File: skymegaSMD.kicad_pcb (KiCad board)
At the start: 2 copper layers, 49 x 49 mm, 56 parts, among them IC1 ATMEGA328P-A, K1 CONN_3, P1 CONN_2, P2 CONN_2, SW1 SWITCH On_Off, SW2 SW_PUSH, SW3 SW_PUSH, U1 MIC5205, X1 16Mhz

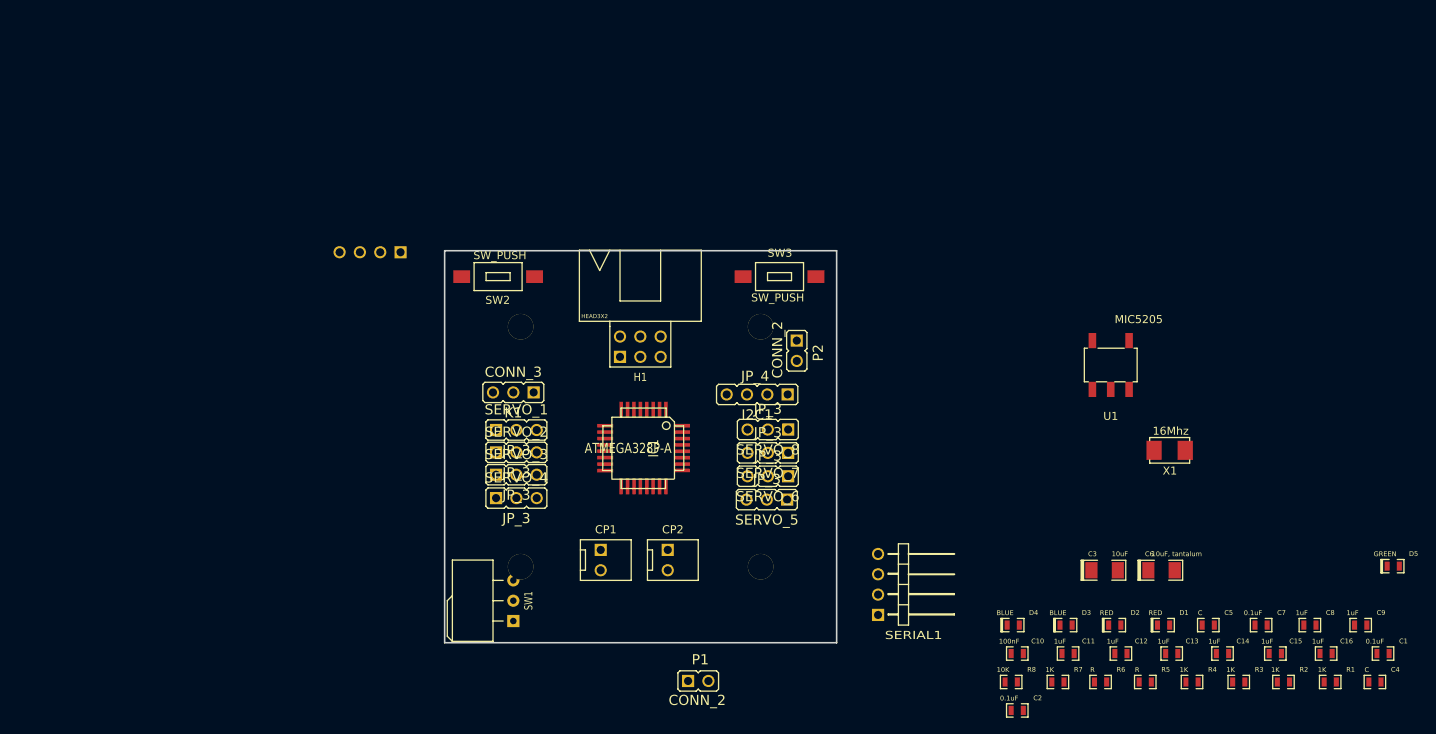
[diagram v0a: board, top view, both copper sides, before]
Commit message: All components placed, capacitors bug solved.
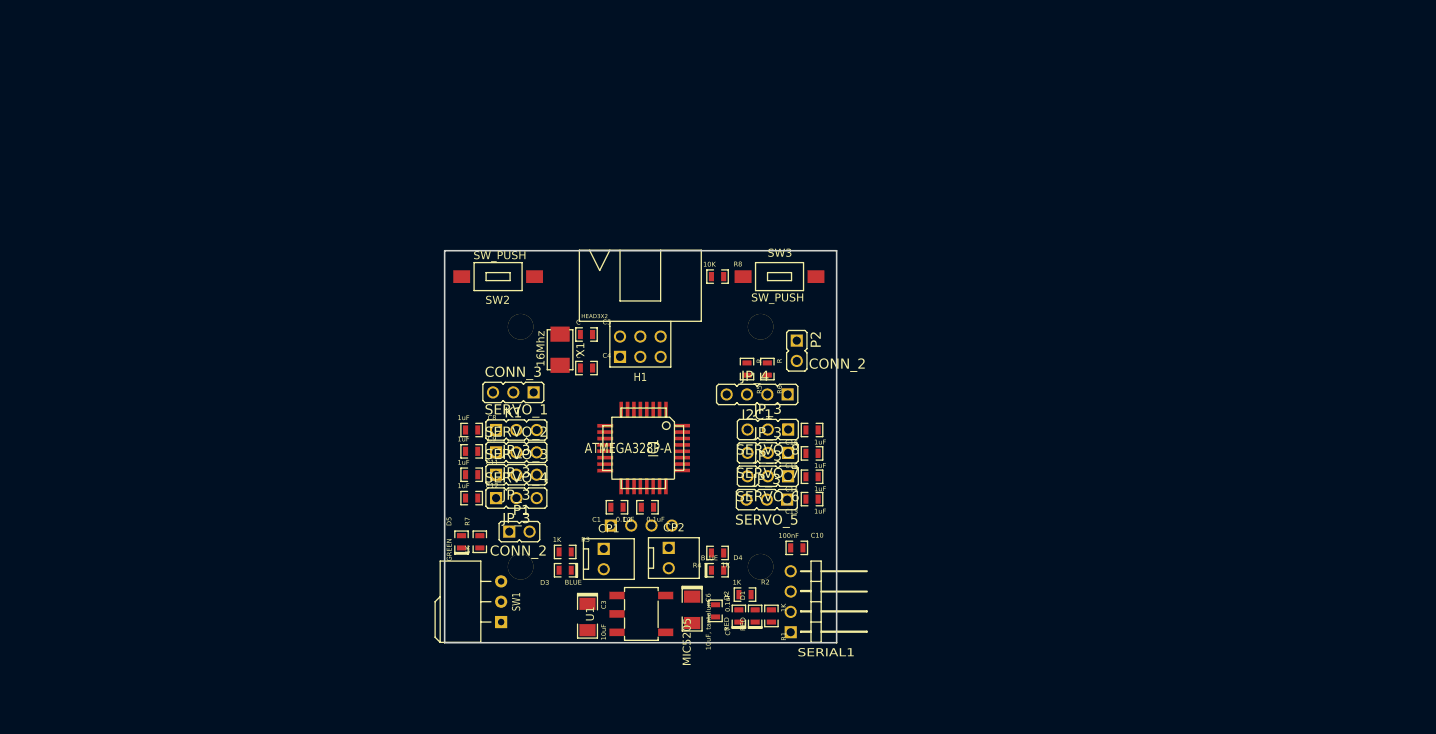
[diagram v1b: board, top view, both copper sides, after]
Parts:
- moved D5 116.5 mm to (175.9, 148.1), turned to 90 degrees
- moved C9 113.2 mm to (177.2, 136.8)
- moved C8 107.6 mm to (177.2, 134.1)
- moved C4 106.1 mm to (191.5, 126.4)
- moved C1 97.5 mm to (195.3, 143.8), turned to 180 degrees
- moved C5 85.8 mm to (191.5, 122.2)
- moved R3 85.8 mm to (188.8, 149.4)
- moved C12 83.4 mm to (177.2, 142.6)
- moved C11 77.8 mm to (177.2, 139.7)
- moved X1 77.2 mm to (188.2, 124.1), turned to 90 degrees
- moved R7 74.4 mm to (178.2, 148.1), turned to 90 degrees
- moved R1 70.3 mm to (214.6, 157.4), turned to 270 degrees
- moved C16 70.1 mm to (219.7, 134.1), turned to 180 degrees
- moved C7 68.2 mm to (207.6, 156.7), turned to 270 degrees
- moved R2 68.2 mm to (211.3, 154.7)
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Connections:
- C13 pad 1: GND -> /Vin
- C14 pad 1: GND -> /Vin
- C8 pad 1: GND -> /Vin
- C9 pad 1: GND -> /Vin

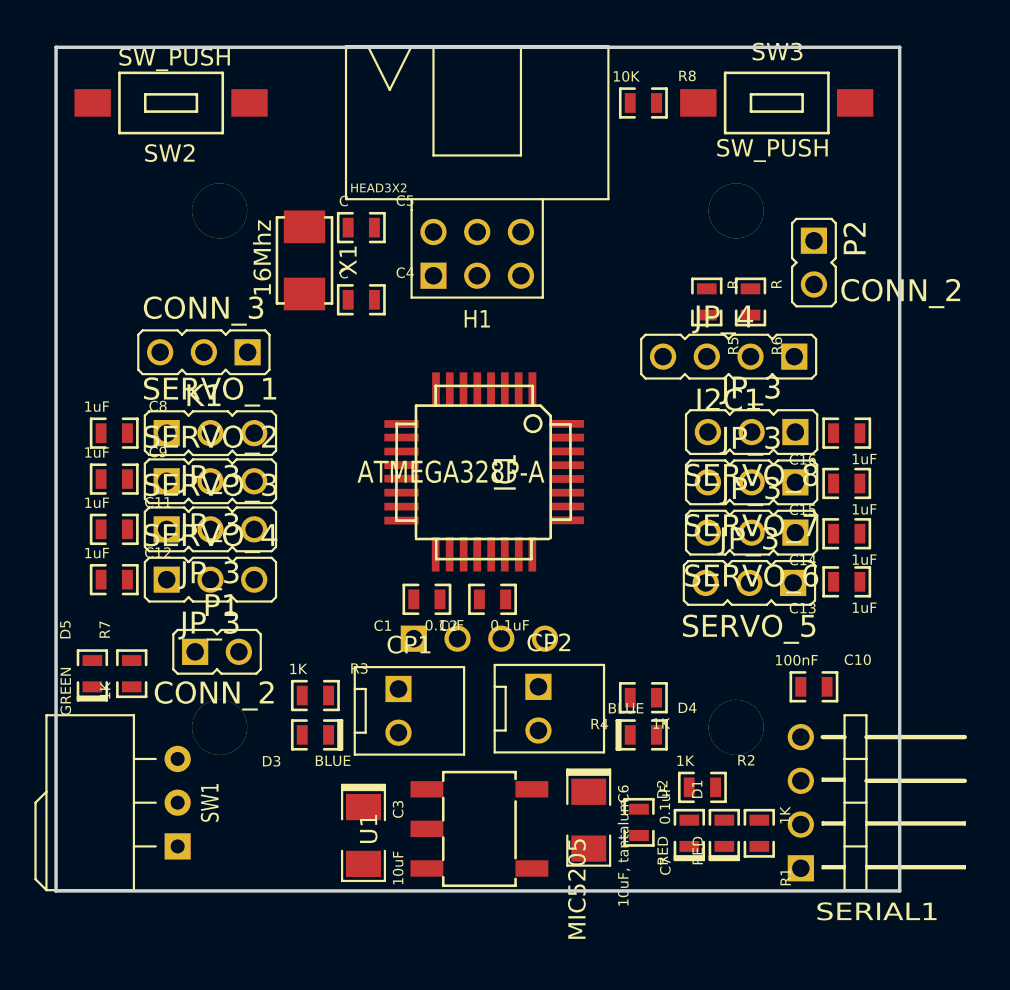
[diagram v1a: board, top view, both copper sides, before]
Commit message: More things routed.
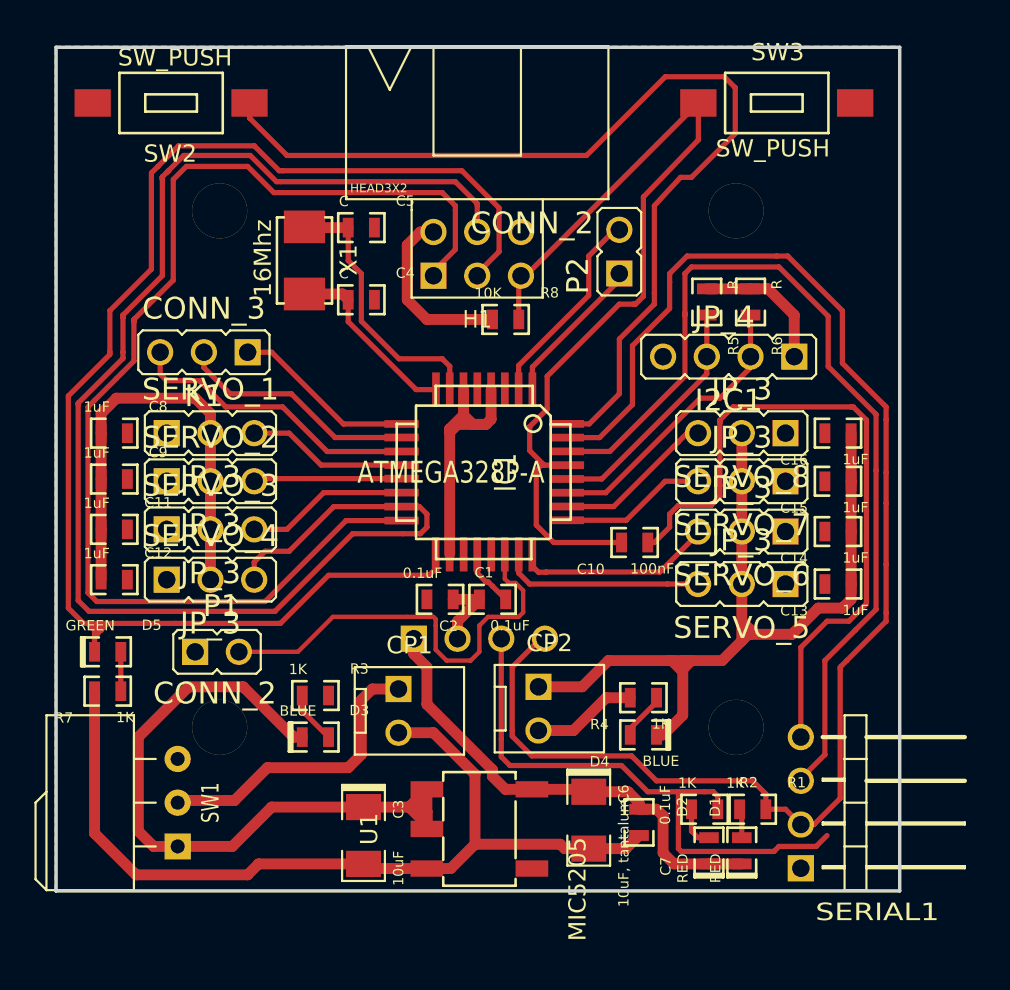
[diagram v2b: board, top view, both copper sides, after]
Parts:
- moved R8 14.9 mm to (199.9, 127.5)
- moved C10 13.4 mm to (207.4, 140.5), turned to 180 degrees
- moved P2 11.5 mm to (206.5, 124.8), turned to 90 degrees
- moved R7 1.73 mm to (176.8, 149.1), turned to 180 degrees
- moved D5 1.55 mm to (176.8, 146.8), turned to 0 degrees
- moved D2 1.53 mm to (211.7, 158.4)
- moved R1 1.45 mm to (214.2, 156.0), turned to 0 degrees
- moved D1 1.44 mm to (213.6, 158.4)
- moved R2 1.28 mm to (211.5, 156.0)
- moved C1 0.76 mm to (196.1, 143.8), turned to 0 degrees
- moved SERVO_6 0.58 mm to (216.2, 139.8)
- moved SERVO_7 0.58 mm to (216.2, 136.9)
- moved SERVO_8 0.58 mm to (216.2, 134.1)
- moved C13 0.52 mm to (219.2, 142.9)
- moved C14 0.52 mm to (219.2, 139.8)
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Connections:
- C13 pad 1: /Vin -> /SERVO_PWR_2
- C14 pad 1: /Vin -> /SERVO_PWR_2
- C15 pad 1: /Vin -> /SERVO_PWR_2
- C16 pad 1: /Vin -> /SERVO_PWR_2
- SERVO_5 pad 2: /Vin -> /SERVO_PWR_2
- SERVO_6 pad 2: /Vin -> /SERVO_PWR_2
- SERVO_7 pad 2: /Vin -> /SERVO_PWR_2
- SERVO_8 pad 2: /Vin -> /SERVO_PWR_2
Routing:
- net /RX: track 0.00 -> 87.9 mm
- net /D11: track 0.00 -> 85.0 mm
- net /TX: track 0.00 -> 84.3 mm
- net /D13: track 0.00 -> 82.6 mm
- net /D12: track 0.00 -> 68.9 mm
- net /Vin: track 0.00 -> 68.2 mm
- net VCC: track 0.00 -> 62.3 mm
- net GND: track 0.00 -> 62.2 mm
- net /D2: track 0.00 -> 56.8 mm
- net /RESET: track 0.00 -> 53.5 mm
- net /SERVO_PWR_2: track 0.00 -> 50.1 mm
- net /DTR: track 0.00 -> 40.2 mm
- net /A7: track 0.00 -> 25.5 mm
- net N-000006: track 0.00 -> 17.4 mm
- net /D7: track 0.00 -> 17.2 mm
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- added copper zone on B.Cu, net GND
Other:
- net class Power added: clearance 0.254, trace_width 0.635, via_dia 0.889, via_drill 0.635
- net class Thick added: clearance 0.254, trace_width 0.3048, via_dia 0.889, via_drill 0.635

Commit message: Only a line left.
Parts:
- moved C1 4.18 mm to (192.2, 145.2), turned to 90 degrees
- moved R8 1.91 mm to (198.0, 127.5)
- moved P1 0.51 mm to (181.9, 147.3)
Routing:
- net GND: track 62.2 -> 235.0 mm
- net VCC: track 62.3 -> 129.4 mm, vias 0 -> 1
- net /A6: track 0.00 -> 19.1 mm
- net /Vin: track 68.2 -> 83.0 mm, vias 0 -> 2
- net /D2: track 56.8 -> 53.8 mm
- net /D13: track 82.6 -> 81.5 mm
- net /RESET: track 53.5 -> 54.5 mm
- net /D12: track 68.9 -> 70.0 mm
- net /D11: track 85.0 -> 86.0 mm

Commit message: Production PCB
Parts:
- added G***: OSHW-logo, OSHW-logo, F.Cu at (125.6, 93.2)
- added G***: LOGO, LOGO_15x15, B.Cu at (145.9, 105.5)
- C6: value 10uF, tantalum -> 10uF
- moved C10 62.0 mm to (152.4, 111.8)
- moved D3 60.2 mm to (136.3, 122.4)
- moved R3 60.2 mm to (136.3, 120.0)
- moved C1 59.9 mm to (139.8, 116.0)
- moved C13 59.9 mm to (166.9, 113.7)
- moved C14 59.9 mm to (166.9, 110.6)
- moved C16 59.9 mm to (166.9, 104.9)
- moved C7 59.9 mm to (155.3, 127.5)
- moved CP1 59.9 mm to (141.4, 119.8)
- moved D1 59.9 mm to (161.3, 129.2)
- moved D2 59.9 mm to (159.4, 129.2)
- moved D4 59.9 mm to (155.6, 122.4)
- moved I2C 59.9 mm to (164.3, 100.5)
- moved K1 59.9 mm to (132.6, 100.2)
- moved P1 59.9 mm to (129.5, 118.1)
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- renumbered I2C1 to I2C
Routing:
- net GND: track 235.0 -> 214.4 mm
- net /RESET: track 54.5 -> 52.1 mm
- net /DTR: track 40.2 -> 42.0 mm
- net /RX: track 87.9 -> 89.6 mm, vias 0 -> 1
- net /Vin: track 83.0 -> 84.7 mm
- net N-0000034: track 10.7 -> 11.2 mm
- added copper zone on F.Cu, net GND
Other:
- outline, holes or cut-outs redrawn
- rule trace_min: 0.254 -> 0.1524
- board text added: "(SCL)A5"
- board text added: "+ Vin -"
- board text added: "+ Vout -"
- board text added: "A0"
- board text added: "A1"
- board text added: "A2"
- board text added: "A3"
- board text added: "A4"
- board text added: "A4(SDA)"
- board text added: "A5"
- board text added: "A6"
- board text added: "A7"
- board text added: "Based on Skymega Board"
- board text added: "CTRL"
- board text added: "D10"
- board text added: "D11"
- board text added: "D12"
- board text added: "D13"
- board text added: "D4"
- board text added: "D5"
- board text added: "D6"
- board text added: "D7"
- board text added: "D8"
- board text added: "D9"
- board text added: "DTR"
- board text added: "Designed by: David Estevez Fernandez"
- board text added: "GND"
- board text added: "GPLv3"
- board text added: "RESET"
- board text added: "RST"
- board text added: "Rx"
- board text added: "SERVO 1"
- board text added: "SERVO 2"
- board text added: "SERVO 3"
- board text added: "SERVO 4"
- board text added: "SERVO5"
- board text added: "SERVO6"
- board text added: "SERVO7"
- board text added: "SERVO8"
- board text added: "SkymegaSMD v1.0 (beta)"
- board text added: "Tx"
- board text added: "USER (D2)"
- board text added: "USER LED"
- board text added: "VCC"
- board text added: "VCC1"
- board text added: "VCC2"
- board text added: "Vin"
- board text added: "www.dsquaredrobotics.com/wiki/doku.php?id=en:repy-2.0"

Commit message: Version presented on thesis.
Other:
- rule pad_to_mask_clearance: 0 -> 0.1
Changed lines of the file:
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@@
     (pad_size 1 1)
     (pad_drill 0.6)
-    (pad_to_mask_clearance 0)
+    (pad_to_mask_clearance 0.1)
+    (solder_mask_min_width 0.1)
     (aux_axis_origin 0 0)
     (visible_elements 7FFFFBBF)
     (pcbplotparams
-      (layerselection 3178497)
+      (layerselection 284196865)
       (usegerberextensions true)
-      (excludeedgelayer true)
-      (linewidth 150000)
+      (excludeedgelayer false)
+      (linewidth 20000)
       (plotframeref false)
       (viasonmask false)
@@
       (plotinvisibletext false)
       (padsonsilk false)
-      (subtractmaskfromsilk false)
+      (subtractmaskfromsilk true)
       (outputformat 1)
       (mirror false)
-      (drillshape 1)
+      (drillshape 0)
       (scaleselection 1)
-      (outputdirectory ""))
+      (outputdirectory Gerbers/))
   )
   (net 0 "")

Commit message: Some bugs solved.
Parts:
- C6: value 10uF -> 10uF, tantalum
- U1: footprint hebi_SOT-223-5 -> hebi_power-SOT-23-5
- moved X1 5.97 mm to (138.8, 100.1), turned to 0 degrees
- moved C5 4.02 mm to (140.5, 96.8), turned to 90 degrees
- moved C6 2.79 mm to (149.6, 127.4)
- moved C7 2.79 mm to (152.5, 127.5)
- moved C3 2.45 mm to (141.6, 127.4)
- moved C4 2.32 mm to (136.9, 96.8), turned to 90 degrees
- moved U1 1.17 mm to (145.3, 127.0)
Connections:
- SW1 pad 3: N-0000036 -> (no net)
- U1 pad 4: N-0000038 -> (no net)
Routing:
- net VCC: track 129.0 -> 120.9 mm
- net N-0000035: track 15.9 -> 7.90 mm
- net /D12: track 70.0 -> 64.4 mm
- net /D11: track 86.0 -> 80.5 mm
- net /D13: track 81.5 -> 76.7 mm
- net /Vin: track 84.7 -> 81.2 mm
- net GND: track 214.4 -> 212.6 mm, vias 0 -> 1
- net /D5: track 10.7 -> 11.2 mm
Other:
- board text added: "+"
- board text added: "-"
- board text removed: "+ Vin -"
- board text removed: "+ Vout -"

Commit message: Edited silkscreen.
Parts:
- moved D1 2.80 mm to (158.5, 129.0), turned to 0 degrees
- moved R2 2.68 mm to (161.8, 127.0)
- moved D2 2.33 mm to (158.5, 127.0), turned to 0 degrees
- moved R1 2.29 mm to (161.8, 129.0)
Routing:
- net /RX: track 89.8 -> 80.9 mm, vias 1 -> 0
- net /TX: track 84.5 -> 87.0 mm, vias 0 -> 1
- net VCC: track 120.9 -> 118.9 mm
- net N-000001: track 2.44 -> 1.78 mm
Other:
- board text added: "More info: www.dsquaredrobotics.com/wiki"
- board text added: "RX"
- board text added: "SERVO 5"
- board text added: "SERVO 6"
- board text added: "SERVO 7"
- board text added: "SERVO 8"
- board text added: "SkymegaSMD v1.1"
- board text added: "TX"
- board text removed: "SERVO5"
- board text removed: "SERVO6"
- board text removed: "SERVO7"
- board text removed: "SERVO8"
- board text removed: "SkymegaSMD v1.0 (beta)"
- board text removed: "www.dsquaredrobotics.com/wiki/doku.php?id=en:repy-2.0"
